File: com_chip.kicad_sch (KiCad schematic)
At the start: 1 part, among them U1 BQ79600PWRQ1

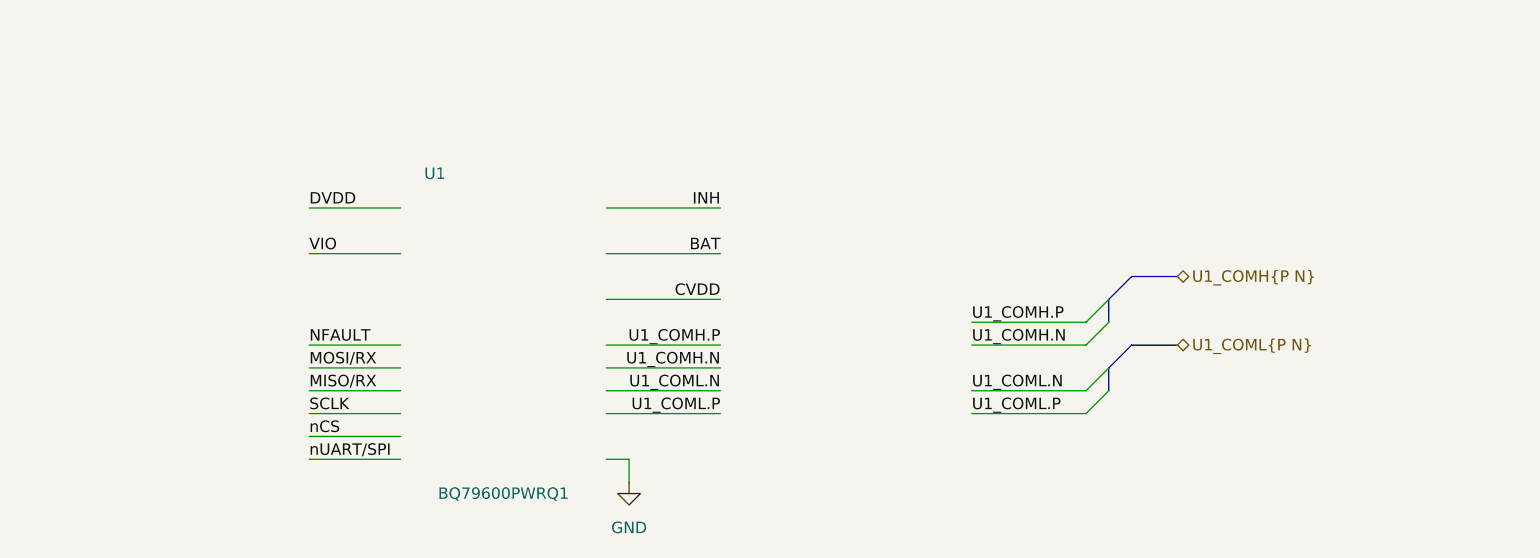
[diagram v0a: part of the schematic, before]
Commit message: SCH[Power]: Adding caps, resistors based off datasheet recs.
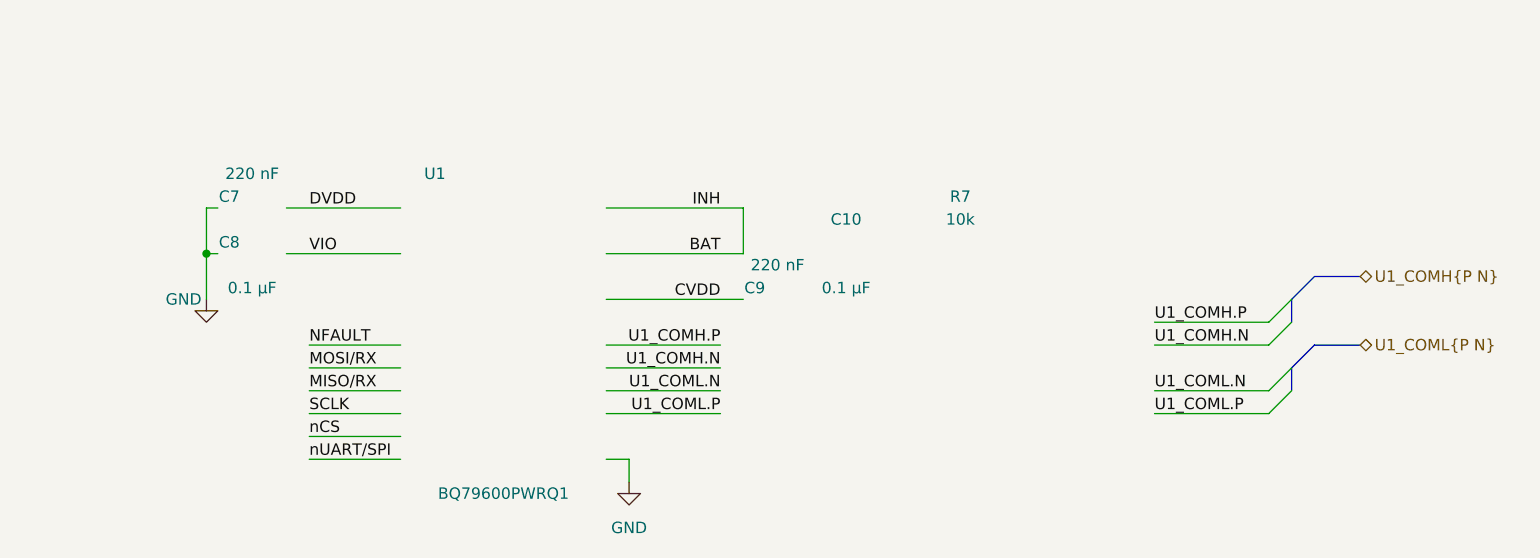
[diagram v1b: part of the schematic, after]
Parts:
- added C10, C8: 0.1 µF, remote_cl05a105ko5nnnc:C_0402_1005Metric, symbol remote_gcm155r71h104ke02j:C
- added C7, C9: 220 nF, remote_cl05a105ko5nnnc:C_0402_1005Metric, symbol remote_grm155r61h224ke01d:C
- added R7: 10k, remote_rcs060359r0fkea:R_0603_1608Metric, symbol remote_rc0402jr-0710kl:RT0402BRD0710KL
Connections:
- net INH is gone; now on net BAT: U1.16 (INH)
- net CVDD: now also C9.1
- net DVDD: now also C7.2
- net GND: now also C7.1, C8.2
- net VIO: now also C8.1

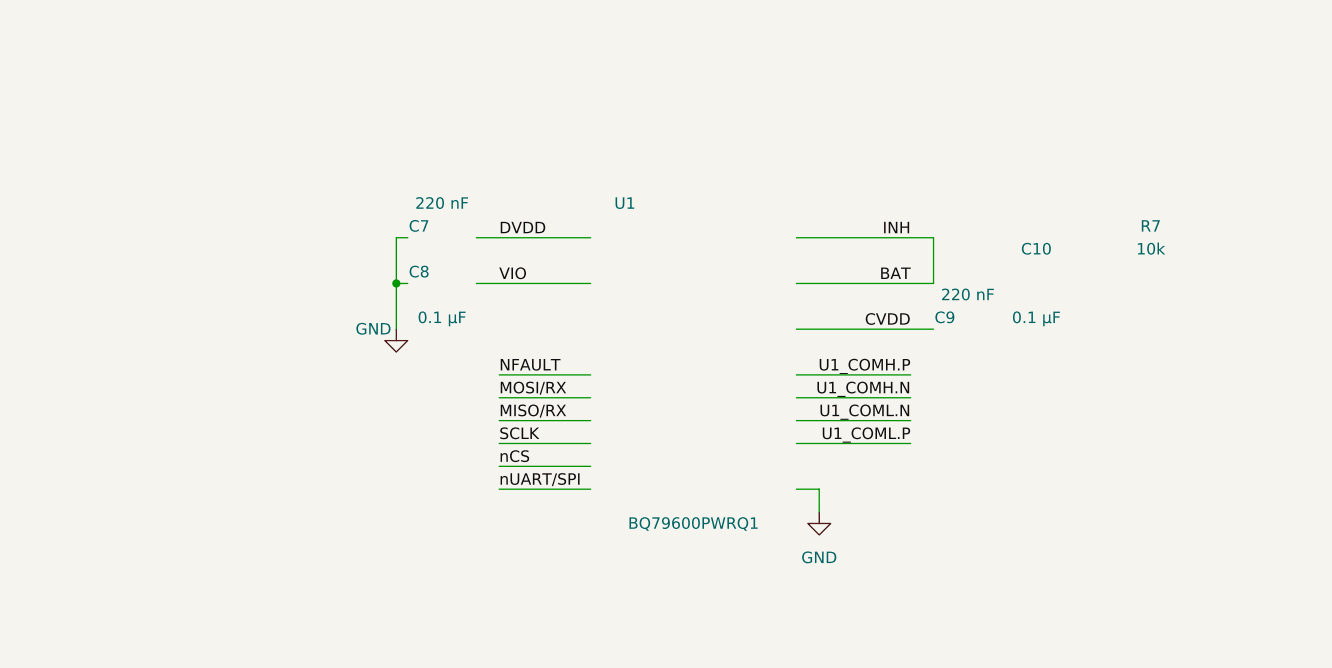
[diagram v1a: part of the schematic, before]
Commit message: SCH[Pages, Chips]: Created page setup, and placed main IC's.
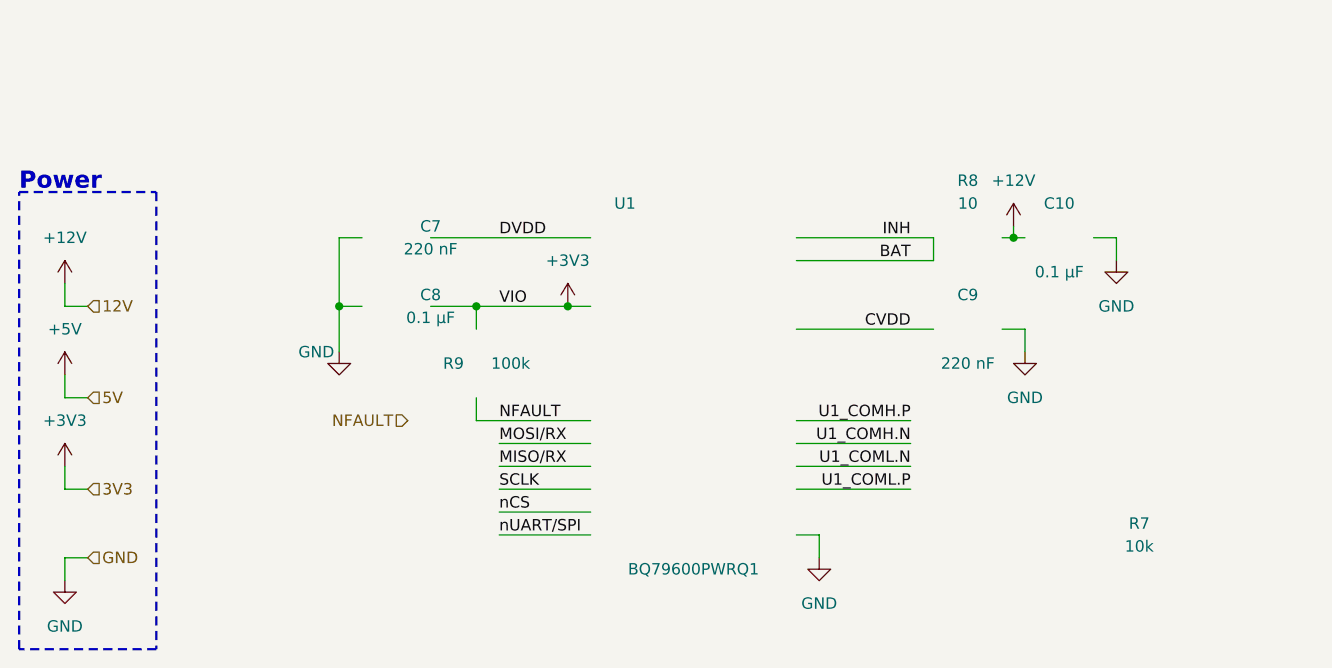
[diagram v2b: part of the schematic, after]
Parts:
- added R8: 10, remote_rcs060359r0fkea:R_0603_1608Metric, symbol remote_crcw060310r0jnea:R_US
- added R9: 100k, remote_rcs060359r0fkea:R_0603_1608Metric, symbol remote_crcw0603100kfkea:R_US
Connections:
- net BAT: now also R8.1
- net GND: now also C10.1, C9.2
- net NFAULT: now also R9.1
- net +12V: now reaches C10.2
- net +12V: now also R8.2
- net VIO renamed +3V3
- net +3V3: now also R9.2
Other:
- note added: "Power"

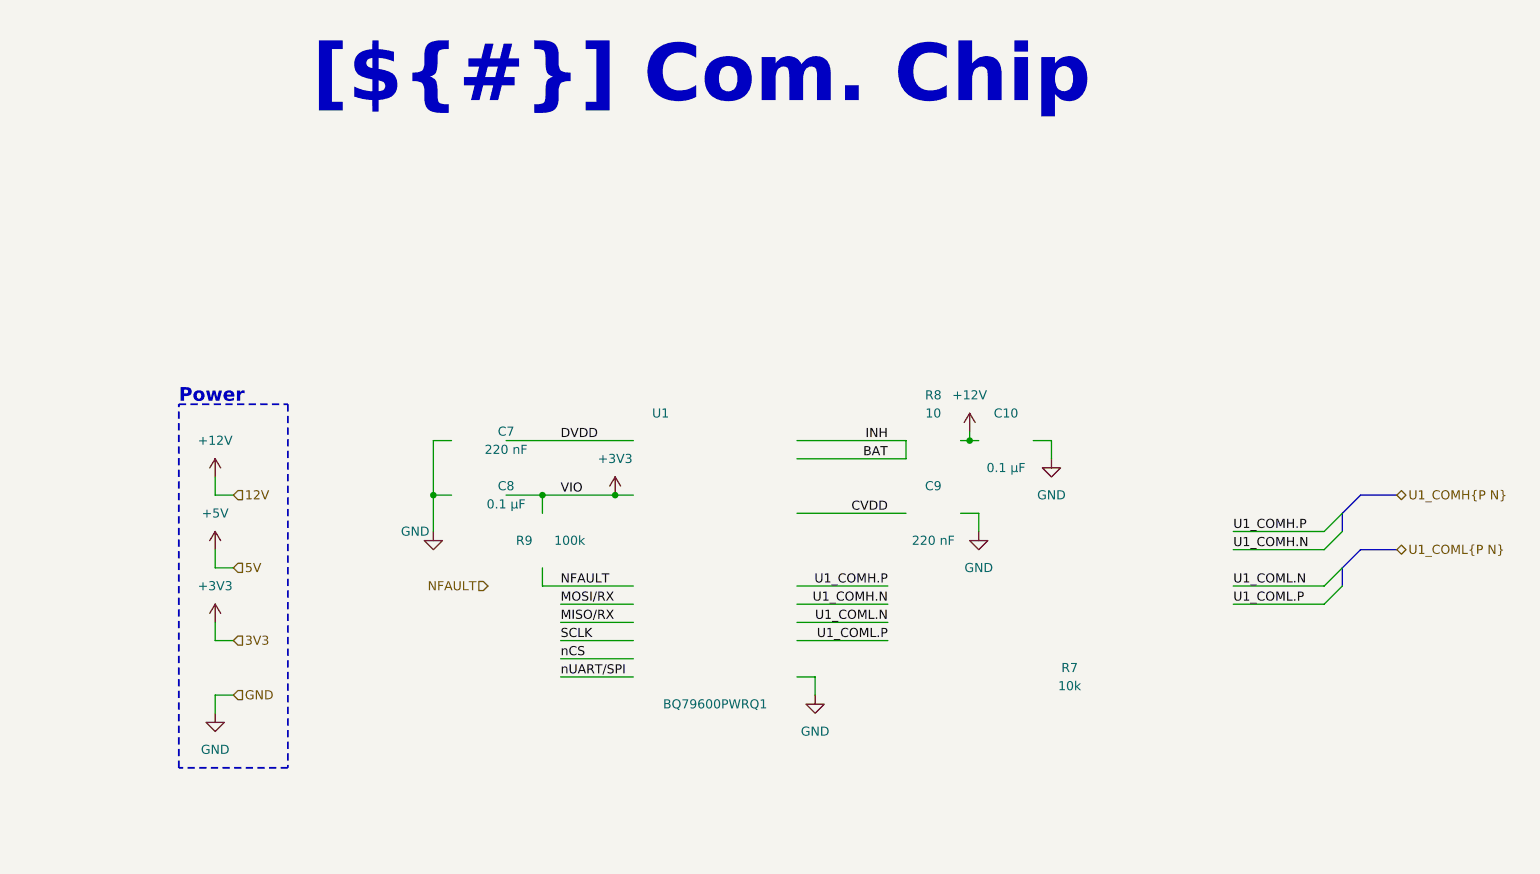
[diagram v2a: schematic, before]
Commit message: SCH[Labels]: Working on pinout for tim.
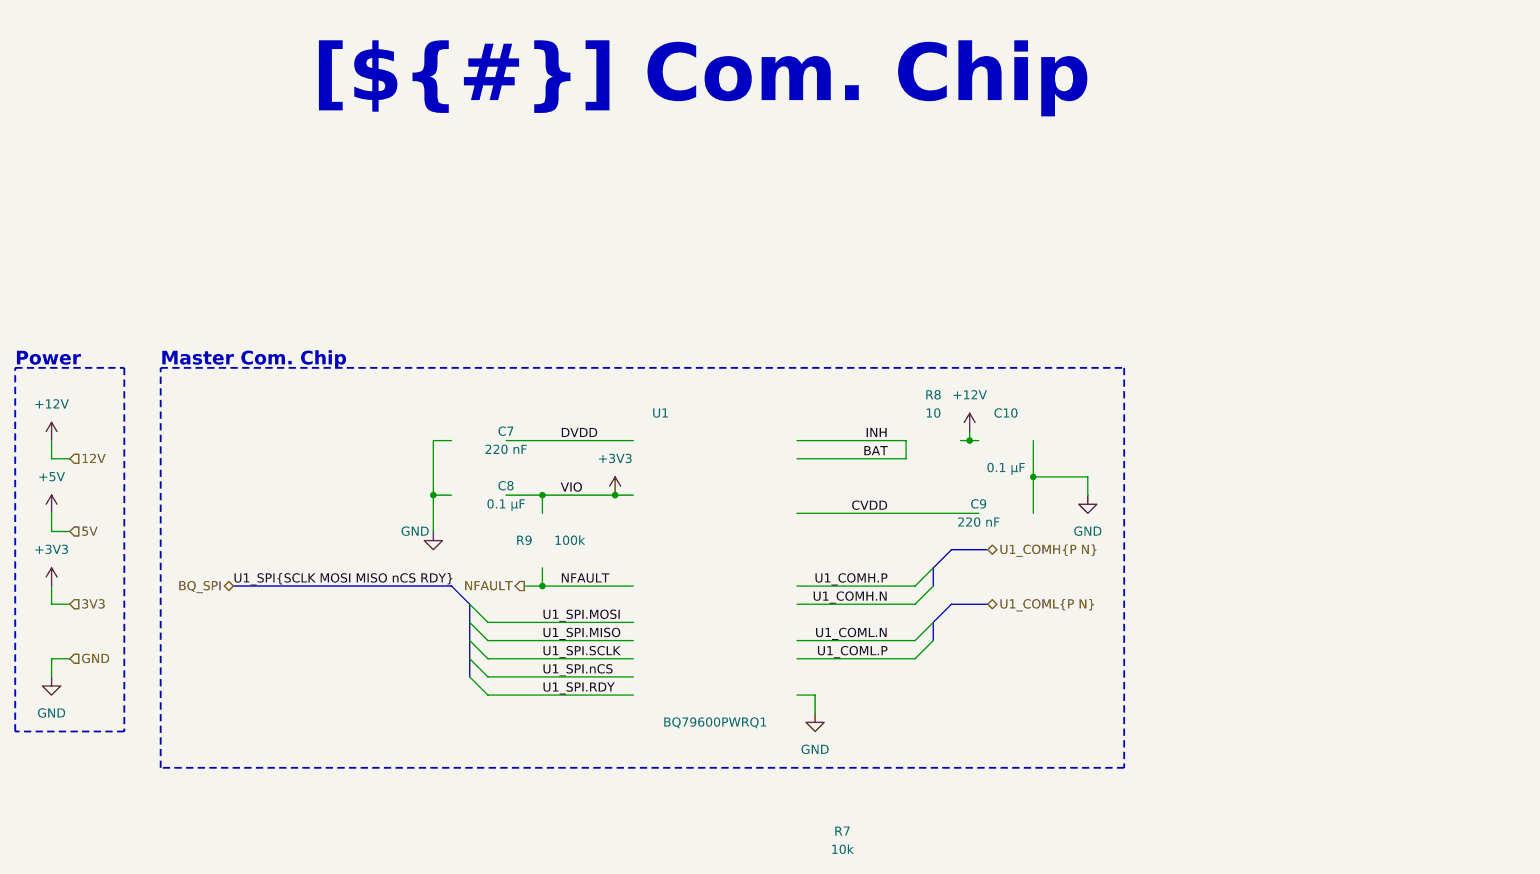
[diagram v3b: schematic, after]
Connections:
- net MISO/RX renamed U1_SPI.MISO
- net MOSI/RX renamed U1_SPI.MOSI
- net SCLK renamed U1_SPI.SCLK
- net nCS renamed U1_SPI.nCS
- net nUART/SPI renamed U1_SPI.RDY
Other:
- note added: "Master Com. Chip"

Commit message: SCH[Sens & Inputs, Logic]: Started on sens and inputs condtiong, Logic page drawn. Need to add notes still.
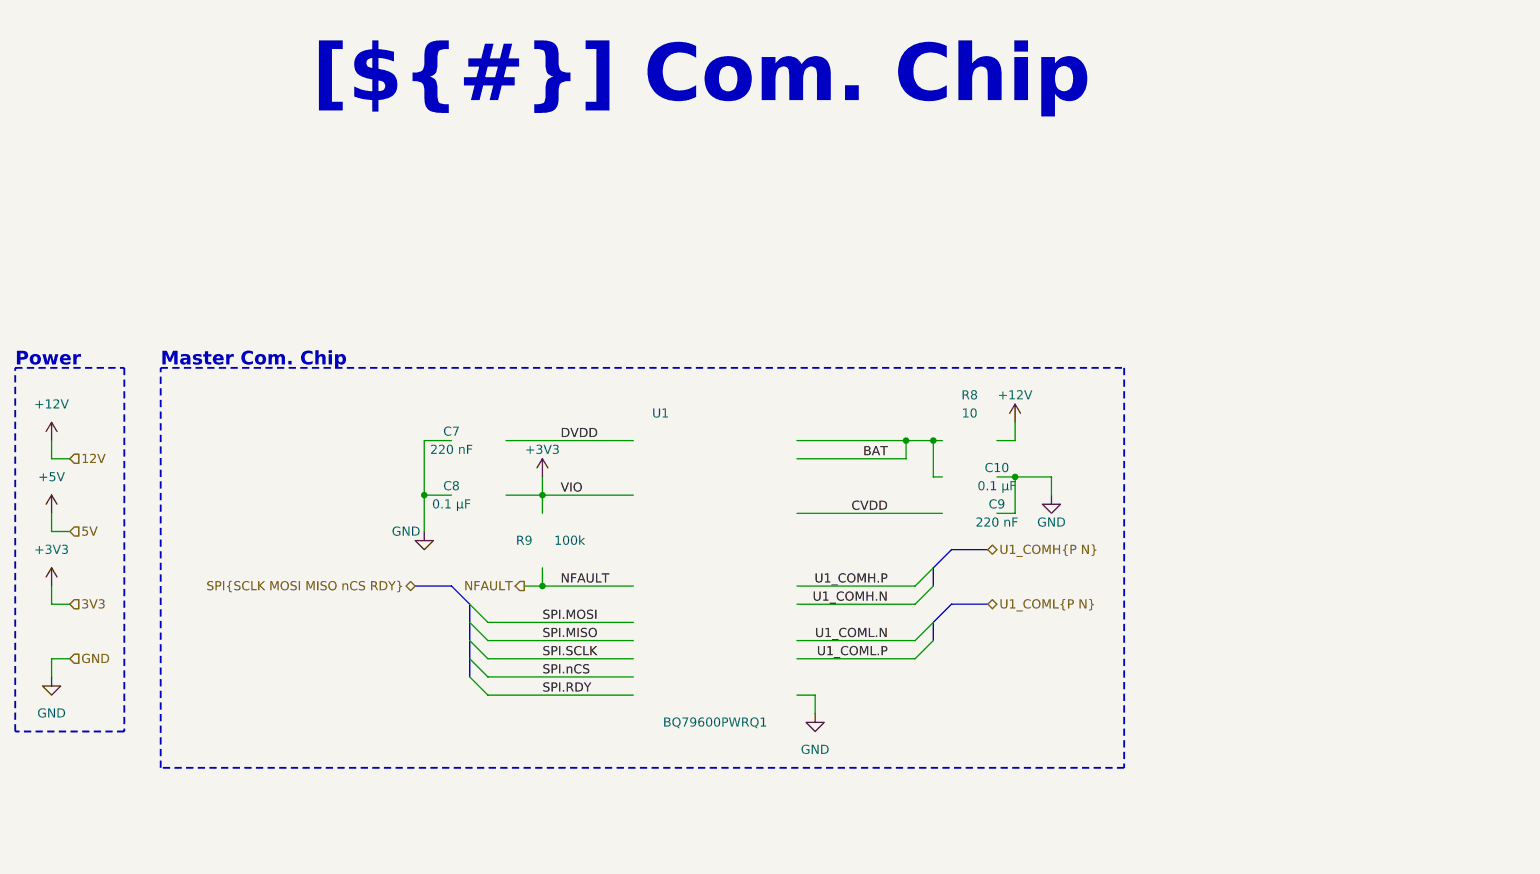
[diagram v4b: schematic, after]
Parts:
- removed R7: 10k, remote_rcs060359r0fkea:R_0603_1608Metric, symbol remote_rc0402jr-0710kl:RT0402BRD0710KL
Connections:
- net +12V: no longer C10.2
- net BAT: now also C10.1
- net GND: now also C10.2; no longer C10.1
- net U1_SPI.MISO renamed SPI.MISO
- net U1_SPI.MOSI renamed SPI.MOSI
- net U1_SPI.RDY renamed SPI.RDY
- net U1_SPI.SCLK renamed SPI.SCLK
- net U1_SPI.nCS renamed SPI.nCS

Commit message: SCH[Logic, Connectors]: Removed watchdog timer going to use just stm32 interal watchdog, and com master faults. This is to simplfiy hardware less parts not needed. Adding DNP conector for halleffect sensor.
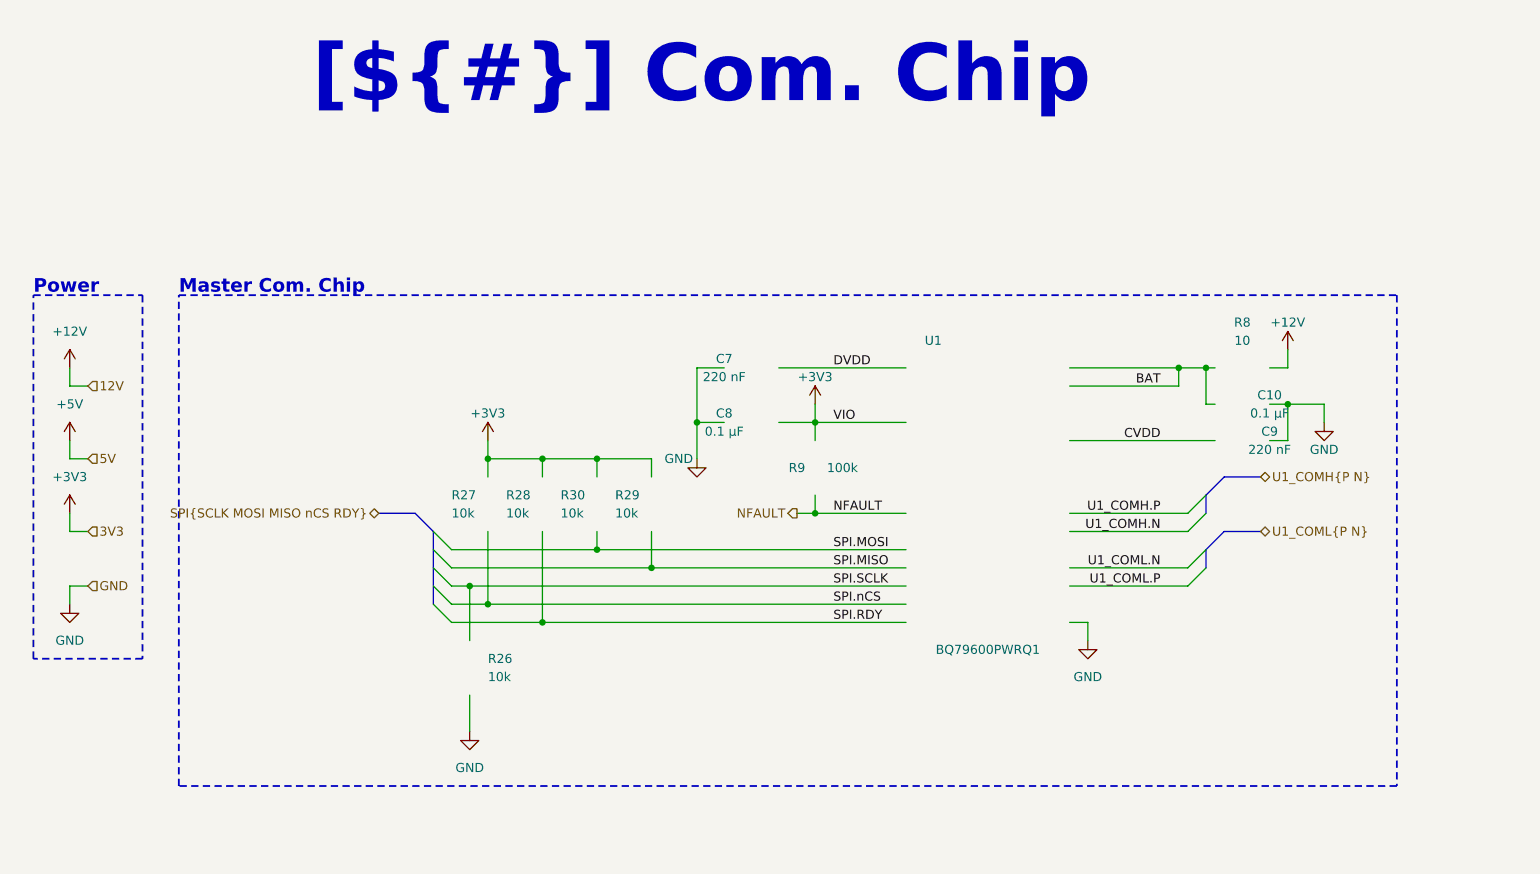
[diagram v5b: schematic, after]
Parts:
- added R26, R27, R28, R29, R30: 10k, remote_erj-2ge0r00x:R_0402_1005Metric, symbol remote_rc0402jr-0710kl:RT0402BRD0710KL
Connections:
- net +3V3: now also R27.2, R28.2, R29.2, R30.2
- net GND: now also R26.1
- net SPI.MISO: now also R29.1
- net SPI.MOSI: now also R30.1
- net SPI.RDY: now also R28.1
- net SPI.SCLK: now also R26.2
- net SPI.nCS: now also R27.1
